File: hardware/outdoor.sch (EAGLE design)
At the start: 31 parts, among them IC1 ATMEGA1284P, IC3 LP2951M, IC6 TS5205, Q1 12MHz

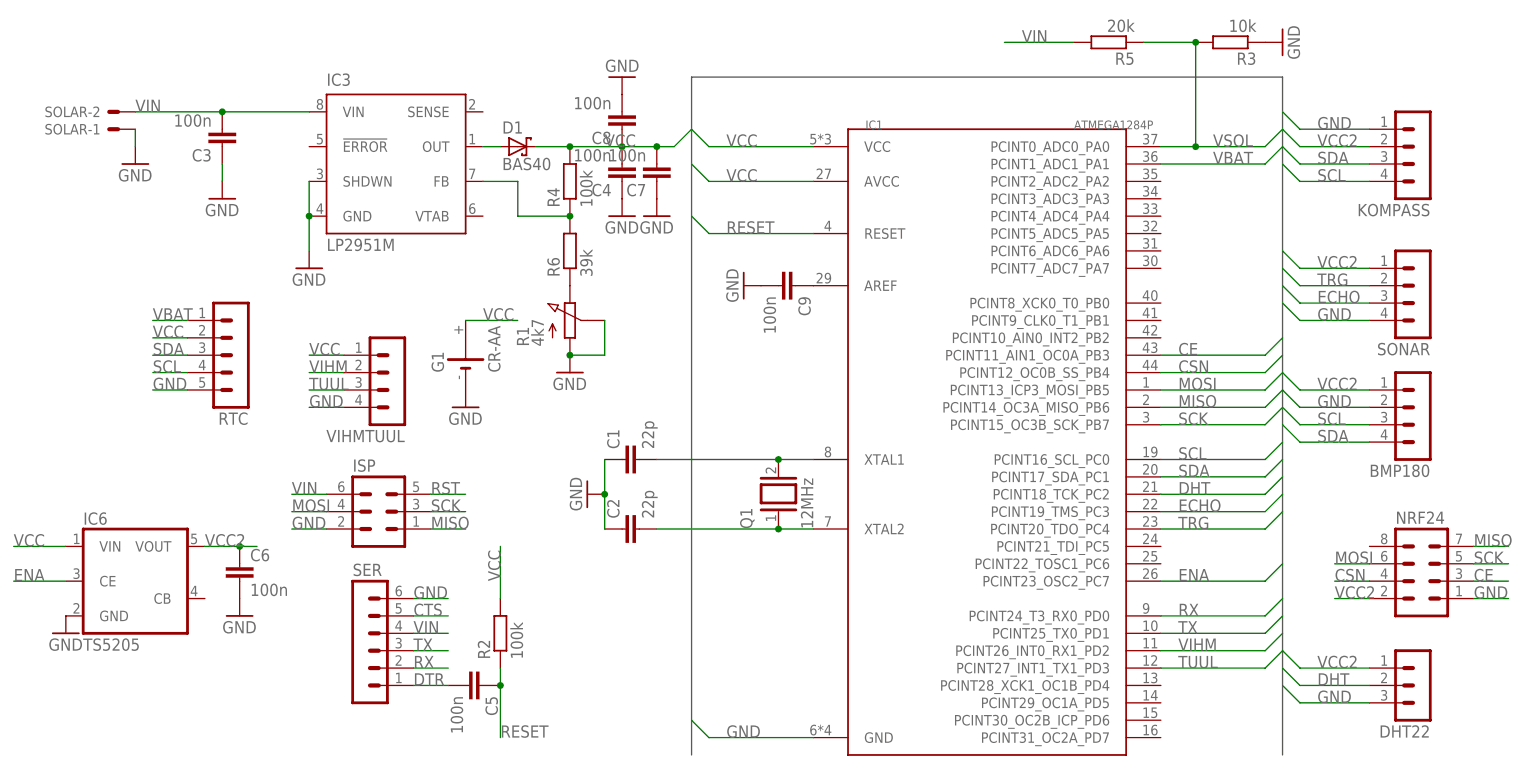
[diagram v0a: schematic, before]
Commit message: Reset switch to schematic
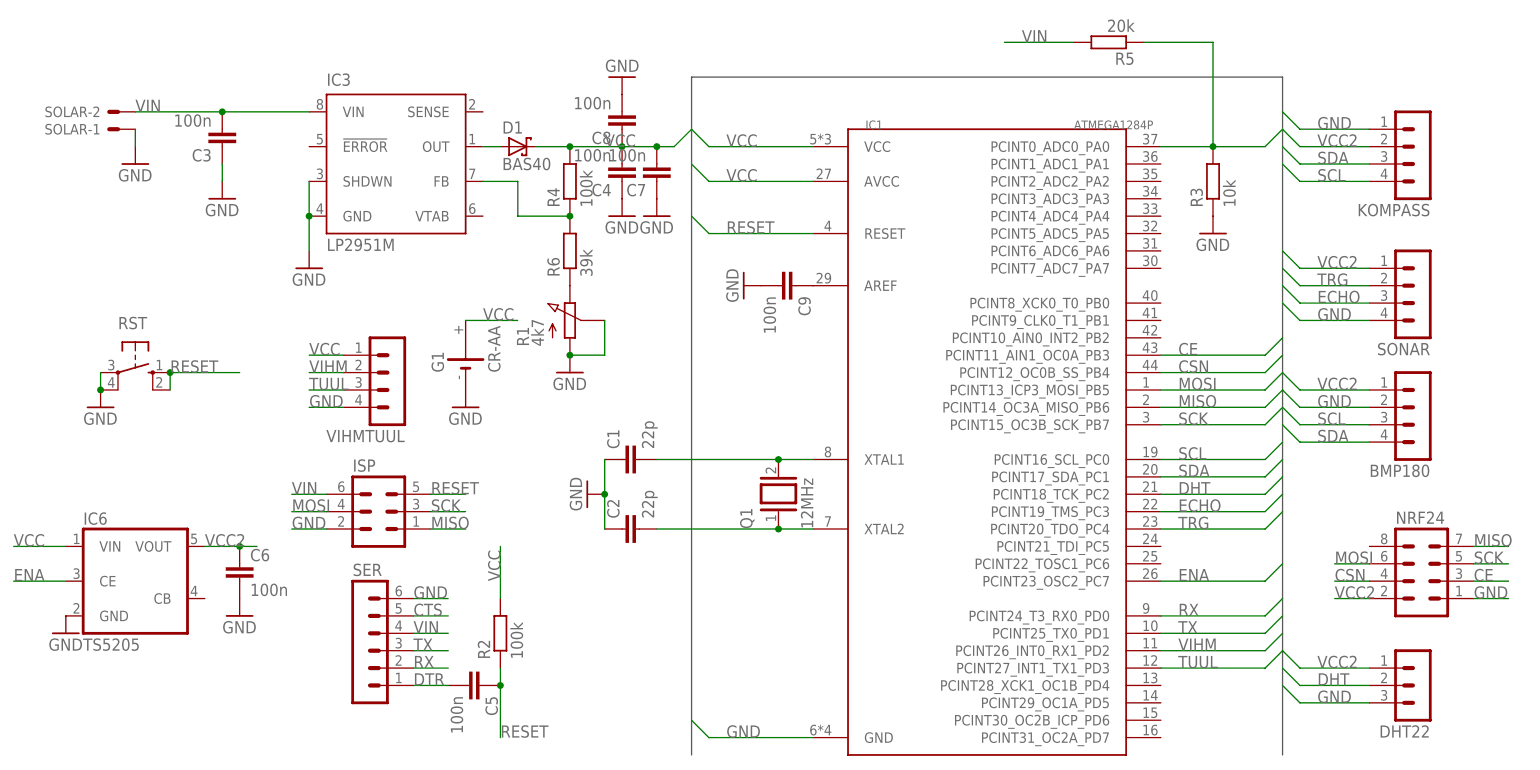
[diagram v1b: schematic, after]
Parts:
- removed RTC: (no value), con-lstb:MA05-1
- added RST: (no value), switch-omron:10-XX
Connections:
- net VSOL renamed B$1
- removed net RST: ISP.5
- removed net VBAT: IC1.PCINT1_ADC1_PA1, RTC.1
- net GND: now also RST.P, RST.P1; no longer RTC.5
- net RESET: now also ISP.5, RST.S, RST.S1
- net SCL: no longer RTC.4
- net SDA: no longer RTC.3
- net VCC: no longer RTC.2
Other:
- moved on the sheet: R3
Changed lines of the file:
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@@
 <part name="C9" library="rcl" deviceset="C-EU" device="C1206K" value="100n"/>
 <part name="GND13" library="supply1" deviceset="GND" device=""/>
-<part name="RTC" library="con-lstb" deviceset="MA05-1" device=""/>
+<part name="RST" library="switch-omron" deviceset="10-XX" device=""/>
+<part name="GND14" library="supply1" deviceset="GND" device=""/>
 </parts>
 <sheets>
@@
 <instance part="C6" gate="G$1" x="-43.18" y="10.16"/>
 <instance part="GND8" gate="1" x="-43.18" y="2.54"/>
-<instance part="R3" gate="G$1" x="101.6" y="86.36" rot="R180"/>
-<instance part="GND10" gate="1" x="109.22" y="86.36" rot="R90"/>
+<instance part="R3" gate="G$1" x="99.06" y="66.04" rot="R90"/>
+<instance part="GND10" gate="1" x="99.06" y="58.42"/>
 <instance part="R5" gate="G$1" x="83.82" y="86.36" rot="R180"/>
 <instance part="C7" gate="G$1" x="17.78" y="66.04" rot="R180"/>
@@
 <instance part="C9" gate="G$1" x="38.1" y="50.8" rot="R270"/>
 <instance part="GND13" gate="1" x="30.48" y="50.8" rot="R270"/>
-<instance part="RTC" gate="G$1" x="-43.18" y="40.64" rot="R180"/>
+<instance part="RST" gate="1" x="-58.42" y="38.1" rot="R270"/>
+<instance part="GND14" gate="1" x="-63.5" y="33.02"/>
 </instances>
 <busses>
@@
 </segment>
 <segment>
-<pinref part="RTC" gate="G$1" pin="5"/>
-<wire x1="-50.8" y1="35.56" x2="-55.88" y2="35.56" width="0.1524" layer="91"/>
-<label x="-55.88" y="35.56" size="1.778" layer="95"/>
+<pinref part="RST" gate="1" pin="P1"/>
+<pinref part="GND14" gate="1" pin="GND"/>
+<pinref part="RST" gate="1" pin="P"/>
+<wire x1="-63.5" y1="35.56" x2="-63.5" y2="38.1" width="0.1524" layer="91"/>
+<junction x="-63.5" y="35.56"/>
 </segment>
 </net>
@@
 <label x="-33.02" y="40.64" size="1.778" layer="95"/>
 </segment>
-<segment>
-<pinref part="RTC" gate="G$1" pin="2"/>
-<wire x1="-50.8" y1="43.18" x2="-55.88" y2="43.18" width="0.1524" layer="91"/>
-<label x="-55.88" y="43.18" size="1.778" layer="95"/>
-</segment>
 </net>
 <net name="RESET" class="0">
@@
 <label x="-5.08" y="-15.24" size="1.778" layer="95"/>
 </segment>
+<segment>
+<pinref part="ISP" gate="1" pin="5"/>
+<wire x1="-15.24" y1="20.32" x2="-10.16" y2="20.32" width="0.1524" layer="91"/>
+<label x="-15.24" y="20.32" size="1.778" layer="95"/>
+</segment>
+<segment>
+<pinref part="RST" gate="1" pin="S"/>
+<junction x="-53.34" y="38.1"/>
+<pinref part="RST" gate="1" pin="S1"/>
+<wire x1="-53.34" y1="35.56" x2="-53.34" y2="38.1" width="0.1524" layer="91"/>
+<wire x1="-53.34" y1="38.1" x2="-43.18" y2="38.1" width="0.1524" layer="91"/>
+<label x="-53.34" y="38.1" size="1.778" layer="95"/>
+</segment>
 </net>
 <net name="SCK" class="0">
@@
 <label x="114.3" y="30.48" size="1.778" layer="95"/>
 </segment>
-<segment>
-<pinref part="RTC" gate="G$1" pin="4"/>
-<wire x1="-50.8" y1="38.1" x2="-55.88" y2="38.1" width="0.1524" layer="91"/>
-<label x="-55.88" y="38.1" size="1.778" layer="95"/>
-</segment>
 </net>
 <net name="SDA" class="0">
@@
 <wire x1="111.76" y1="27.94" x2="109.22" y2="30.48" width="0.1524" layer="91"/>
 <label x="114.3" y="27.94" size="1.778" layer="95"/>
-</segment>
-<segment>
-<pinref part="RTC" gate="G$1" pin="3"/>
-<wire x1="-50.8" y1="40.64" x2="-55.88" y2="40.64" width="0.1524" layer="91"/>
-<label x="-55.88" y="40.64" size="1.778" layer="95"/>
 </segment>
 </net>
@@
 </segment>
 </net>
-<net name="RST" class="0">
-<segment>
-<pinref part="ISP" gate="1" pin="5"/>
-<wire x1="-15.24" y1="20.32" x2="-10.16" y2="20.32" width="0.1524" layer="91"/>
-<label x="-15.24" y="20.32" size="1.778" layer="95"/>
-</segment>
-</net>
 <net name="DTR" class="0">
 <segment>
@@
 </segment>
 </net>
-<net name="VSOL" class="0">
+<net name="B$1" class="0">
 <segment>
 <pinref part="IC1" gate="G$1" pin="PCINT0_ADC0_PA0"/>
-<wire x1="91.44" y1="71.12" x2="96.52" y2="71.12" width="0.1524" layer="91"/>
-<wire x1="96.52" y1="86.36" x2="96.52" y2="71.12" width="0.1524" layer="91"/>
-<wire x1="96.52" y1="71.12" x2="106.68" y2="71.12" width="0.1524" layer="91"/>
+<wire x1="91.44" y1="71.12" x2="99.06" y2="71.12" width="0.1524" layer="91"/>
+<wire x1="99.06" y1="71.12" x2="106.68" y2="71.12" width="0.1524" layer="91"/>
 <wire x1="106.68" y1="71.12" x2="109.22" y2="73.66" width="0.1524" layer="91"/>
 <pinref part="R3" gate="G$1" pin="2"/>
-<junction x="96.52" y="86.36"/>
+<junction x="99.06" y="71.12"/>
 <pinref part="R5" gate="G$1" pin="1"/>
-<wire x1="88.9" y1="86.36" x2="96.52" y2="86.36" width="0.1524" layer="91"/>
-<junction x="96.52" y="71.12"/>
-<label x="99.06" y="71.12" size="1.778" layer="95"/>
+<wire x1="88.9" y1="86.36" x2="99.06" y2="86.36" width="0.1524" layer="91"/>
+<wire x1="99.06" y1="86.36" x2="99.06" y2="71.12" width="0.1524" layer="91"/>
 </segment>
 </net>
@@
 </segment>
 </net>
-<net name="VBAT" class="0">
-<segment>
-<pinref part="IC1" gate="G$1" pin="PCINT1_ADC1_PA1"/>
-<wire x1="91.44" y1="68.58" x2="106.68" y2="68.58" width="0.1524" layer="91"/>
-<wire x1="106.68" y1="68.58" x2="109.22" y2="71.12" width="0.1524" layer="91"/>
-<label x="99.06" y="68.58" size="1.778" layer="95"/>
-</segment>
-<segment>
-<pinref part="RTC" gate="G$1" pin="1"/>
-<wire x1="-50.8" y1="45.72" x2="-55.88" y2="45.72" width="0.1524" layer="91"/>
-<label x="-55.88" y="45.72" size="1.778" layer="95"/>
-</segment>
-</net>
